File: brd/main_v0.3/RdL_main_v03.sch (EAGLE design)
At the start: 33 parts, among them U1 MPU-6000QFN-24

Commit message: Version Ready for fabrication
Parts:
- removed TEST: PRG, SparkFun-Connectors:M01POGOPIN_HOLE_0.58
- added J1: Test, SparkFun-Connectors:M01PTH
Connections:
- net N$4: now also J1.1; no longer TEST.1
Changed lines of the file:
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@@
 <classes>
 <class number="0" name="default" width="0" drill="0">
+<clearance class="0" value="0.205"/>
 </class>
 </classes>
@@
 <part name="D1" library="SparkFun-LED" deviceset="LED-RED" device="1206" value="RED"/>
 <part name="D2" library="SparkFun-LED" deviceset="LED-RED" device="1206" value="RED"/>
-<part name="TEST" library="SparkFun-Connectors" deviceset="M01" device="POGOPIN_HOLE_0.58" value="PRG"/>
 <part name="U$1" library="TLV61225DCKT" deviceset="TLV61225" device=""/>
 <part name="P+3" library="supply1" deviceset="VCC" device=""/>
@@
 <part name="J2" library="SparkFun-Connectors" deviceset="USB-AB" device=""/>
 <part name="GND12" library="supply1" deviceset="GND" device=""/>
+<part name="J1" library="SparkFun-Connectors" deviceset="M01" device="PTH" value="Test"/>
 </parts>
 <sheets>
@@
 <instance part="D1" gate="G$1" x="0" y="96.52" rot="R90"/>
 <instance part="D2" gate="G$1" x="0" y="81.28" rot="R90"/>
-<instance part="TEST" gate="G$1" x="142.24" y="111.76" rot="R270"/>
 <instance part="U$1" gate="G$1" x="58.42" y="20.32"/>
 <instance part="P+3" gate="VCC" x="104.14" y="25.4" rot="R270"/>
@@
 <instance part="J2" gate="G$1" x="-10.16" y="165.1"/>
 <instance part="GND12" gate="1" x="-5.08" y="175.26" rot="R180"/>
+<instance part="J1" gate="G$1" x="142.24" y="109.22" rot="R270"/>
 </instances>
 <busses>
@@
 <pinref part="U$3" gate="G$1" pin="17"/>
 <wire x1="132.08" y1="96.52" x2="142.24" y2="96.52" width="0.1524" layer="91"/>
-<wire x1="142.24" y1="96.52" x2="142.24" y2="104.14" width="0.1524" layer="91"/>
-<pinref part="TEST" gate="G$1" pin="1"/>
-</segment>
-</net>
+<wire x1="142.24" y1="96.52" x2="142.24" y2="101.6" width="0.1524" layer="91"/>
+<pinref part="J1" gate="G$1" pin="1"/>
+</segment>
+</net>

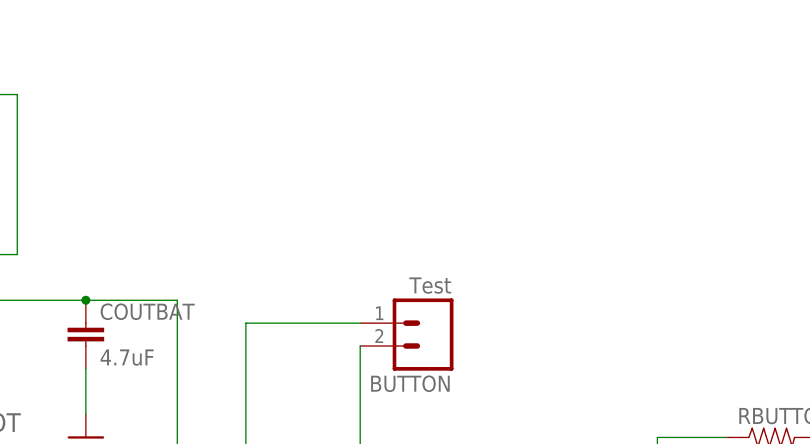
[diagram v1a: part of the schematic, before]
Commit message: Added version 4 to divide in 3 boards
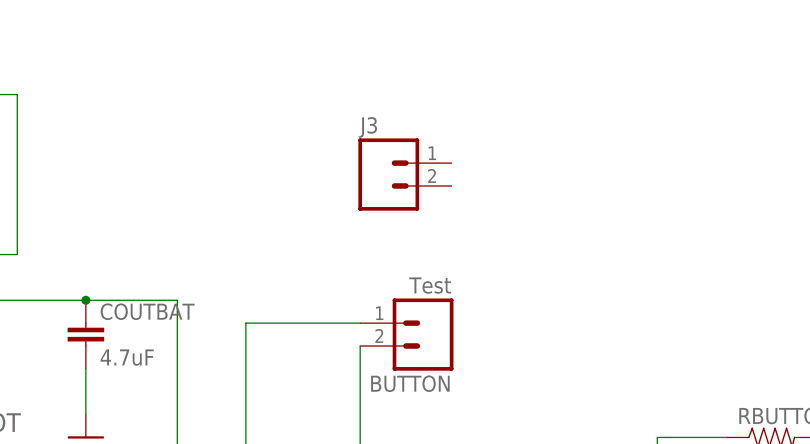
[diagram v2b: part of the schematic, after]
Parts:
- added J3: (no value), SparkFun-Connectors:M02-JST-2MM-SMT
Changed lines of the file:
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@@
 <part name="GND12" library="supply1" deviceset="GND" device=""/>
 <part name="J1" library="SparkFun-Connectors" deviceset="M01" device="PTH" value="Test"/>
+<part name="J3" library="SparkFun-Connectors" deviceset="M02" device="-JST-2MM-SMT"/>
 </parts>
 <sheets>
@@
 <instance part="GND12" gate="1" x="-5.08" y="175.26" rot="R180"/>
 <instance part="J1" gate="G$1" x="142.24" y="109.22" rot="R270"/>
+<instance part="J3" gate="G$1" x="86.36" y="160.02"/>
 </instances>
 <busses>
